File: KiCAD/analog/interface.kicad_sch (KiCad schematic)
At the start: 13 parts, among them J15 Screw_Terminal_01x03, J4 8P8C_Shielded, U16 AM26LS32ACN

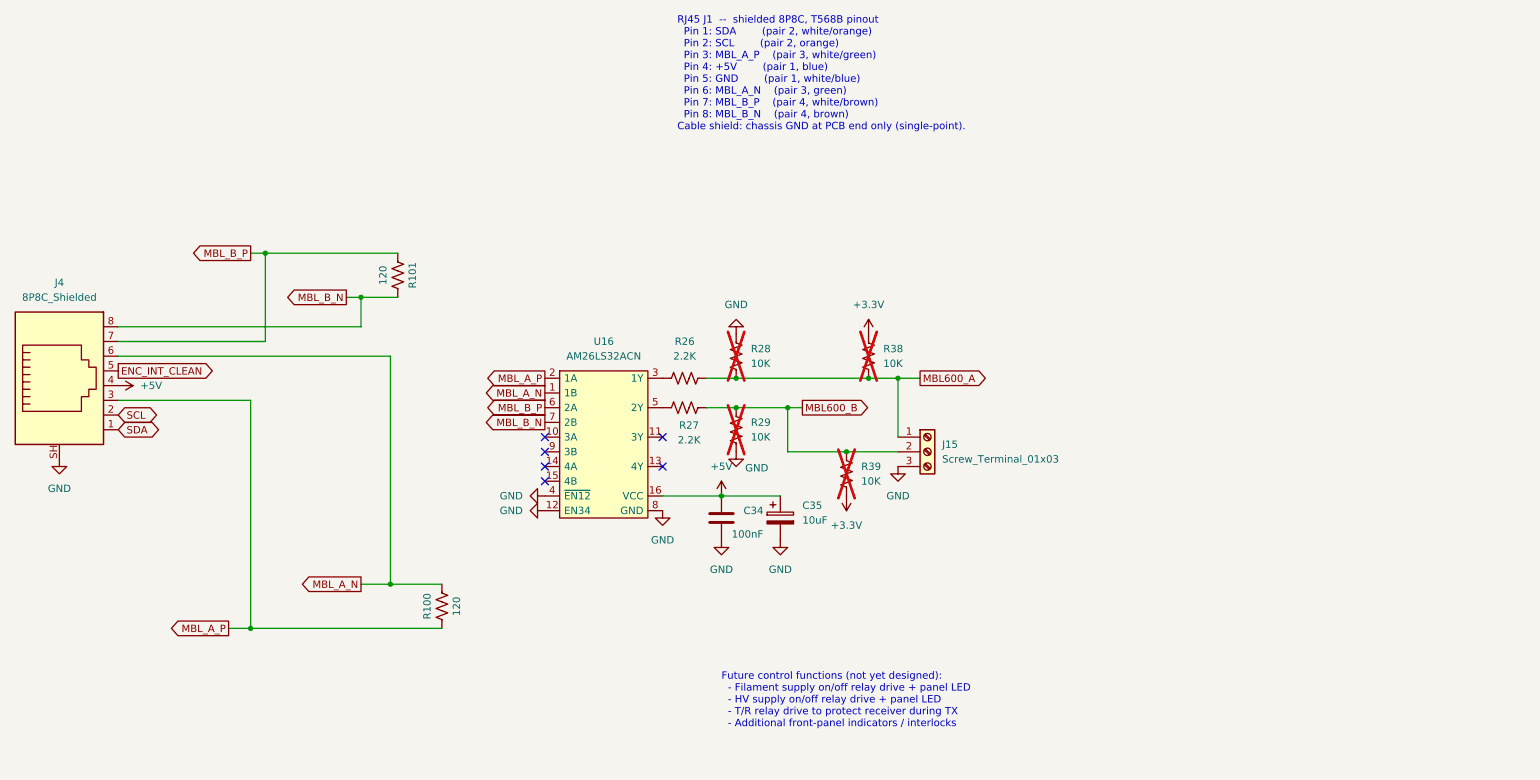
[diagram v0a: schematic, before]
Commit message: revD analog: L1 Bourns 78F footprint + CD74HC4050E xmitter lib additions
Analog L1 (270nH Bourns 78F RF choke) gets footprint
Inductor_THT:L_Axial_L7.0mm_D3.3mm_P10.16mm_Horizontal_Fastron_MICC
(stock KiCad; 78F body 7.11x2.79mm fits within the MICC silk envelope).

Added to xmitter library:
- symbol CD74HC4050E (hex non-inverting buffer, DIP-16, standard 4050
  pinout, pre-linked to xmitter:DIP-16_W7.62mm footprint)
- footprint xmitter:DIP-16_W7.62mm (verbatim copy of stock
  Package_DIP:DIP-16_W7.62mm so the lib is self-contained)

Other sheet / project / netlist touches picked up from the recent
session work on analog test sheet and protoshield.

Co-Authored-By: Claude Opus 4.7 <noreply@anthropic.com>
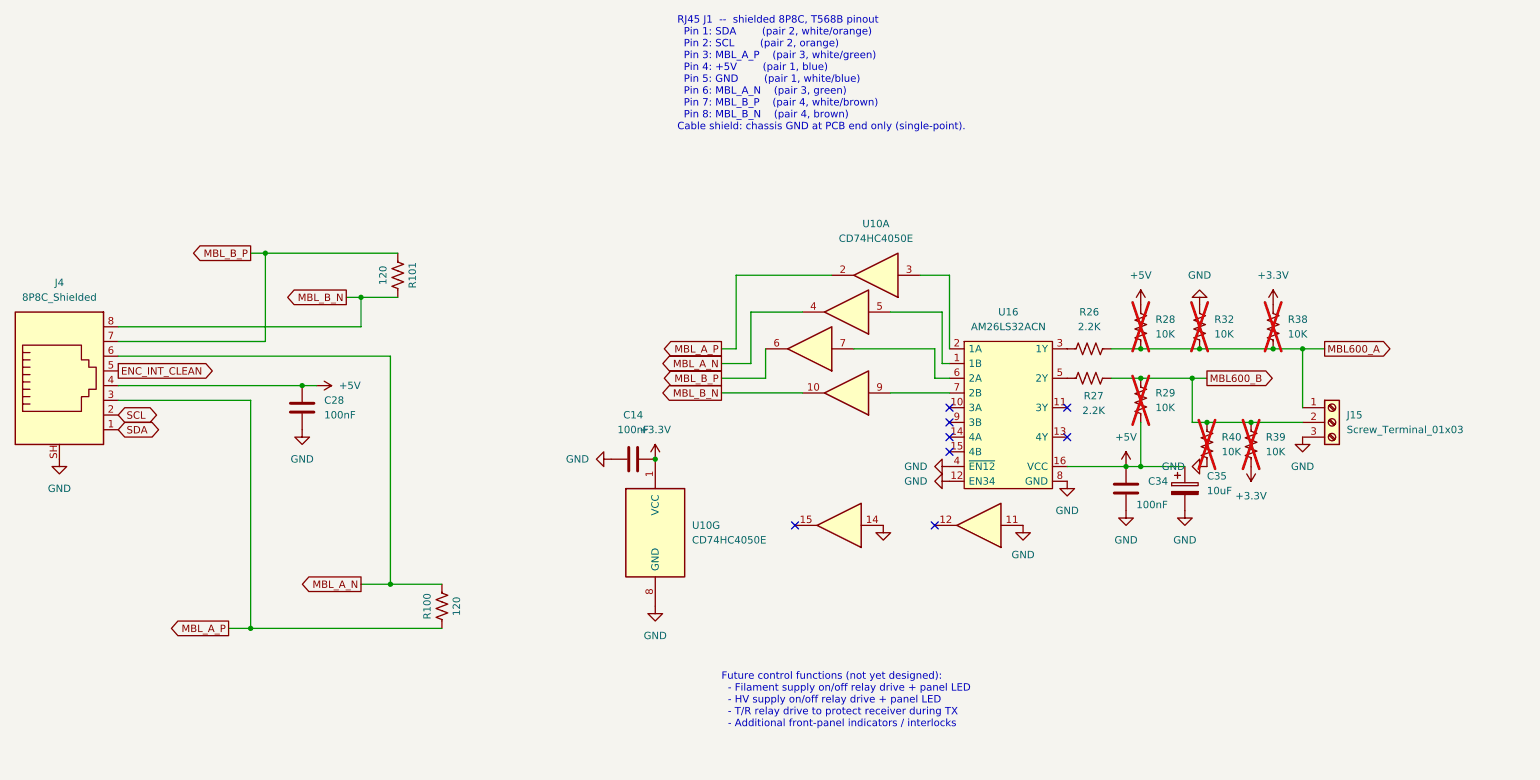
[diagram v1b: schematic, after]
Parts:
- added C14, C28: 100nF, symbol Device:C
- added R32, R40: 10K, Resistor_THT:R_Axial_DIN0207_L6.3mm_D2.5mm_P10.16mm_Horizontal, symbol Device:R_US
- added U10: CD74HC4050E, xmitter:DIP-16_W7.62mm, symbol xmitter:CD74HC4050E
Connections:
- net +3.3V: now also C14.2, U10.1 (VCC)
- net +5V: now also R28.1, R29.2, C28.1
- net GND: now also C14.1, C28.2, R32.1, R40.2, U10.11, U10.14, U10.8 (GND); no longer R28.1, R29.2
- net MBL600_A: now also R32.2
- net MBL600_B: now also R40.1
- net MBL_A_N: now also U10.4; no longer U16.1 (1B)
- net MBL_A_P: now also U10.2; no longer U16.2 (1A)
- net MBL_B_N: now also U10.10; no longer U16.7 (2B)
- net MBL_B_P: now also U10.6; no longer U16.6 (2A)
- new net: U10.3, U16.2 (1A)
- new net: U10.9, U16.7 (2B)
- new net: U10.5, U16.1 (1B)
- new net: U10.7, U16.6 (2A)
- no-connect marks 6 -> 8
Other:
- moved on the sheet: C34, C35, J15, R26, R27, R28, R29, R38, R39, U16

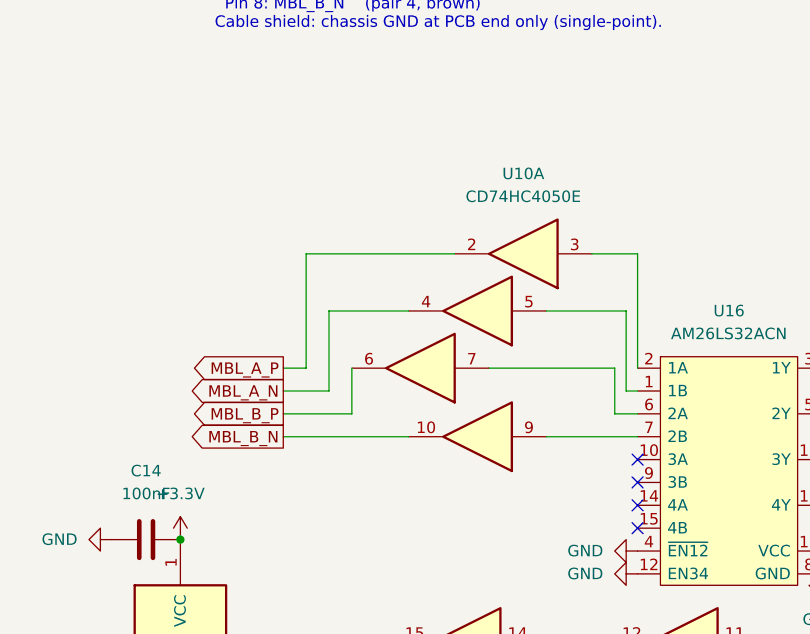
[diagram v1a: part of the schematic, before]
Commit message: revD: ss_pa U13 LM2936 pinout fix + analog U9 74HCT125 miswiring fix
ss_pa fault_shutdown.kicad_sch: fix U13 pin-to-signal mapping so an
LM2936Z-5.0/NOPB can be installed without destruction (prior MCP1700
symbol had pin 1=GND, 2=VI, 3=VO; LM2936 datasheet is pin 1=VO, 2=GND,
3=VI).

analog dac.kicad_sch: fix U9 74HCT125 miswiring found during follow-up
audit.

Co-Authored-By: Claude Opus 4.7 <noreply@anthropic.com>
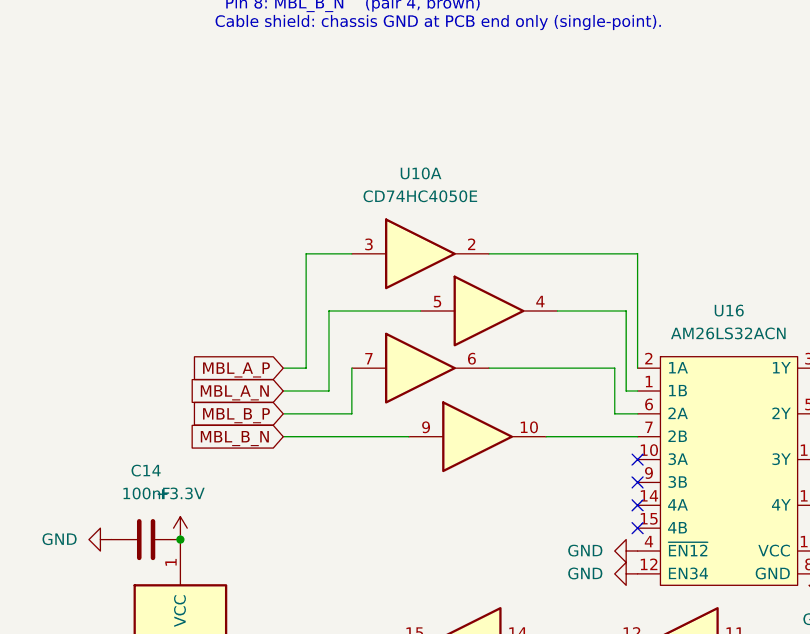
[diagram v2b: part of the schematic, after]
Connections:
- net MBL_A_N: now also U10.5; no longer U10.4
- net MBL_A_P: now also U10.3; no longer U10.2
- net MBL_B_N: now also U10.9; no longer U10.10
- net MBL_B_P: now also U10.7; no longer U10.6
- net at U16.2 (1A): now also U10.2; no longer U10.3
- net at U16.7 (2B): now also U10.10; no longer U10.9
- net at U16.1 (1B): now also U10.4; no longer U10.5
- net at U16.6 (2A): now also U10.6; no longer U10.7

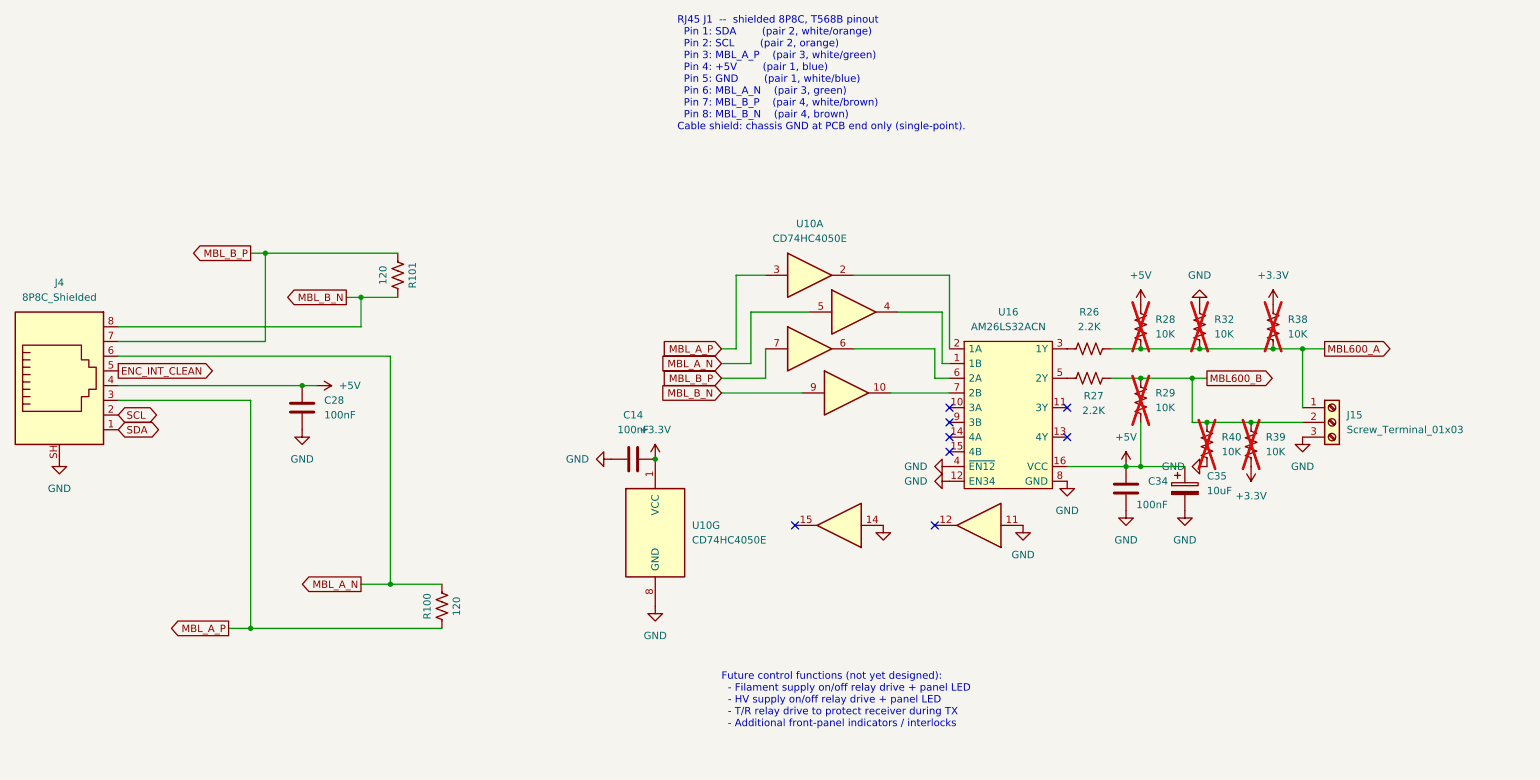
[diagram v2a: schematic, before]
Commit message: revD: footprint pass across all boards + ss_pa fault-chain fix + LLM review brief
- New tools/assign_misc_footprints.py: lib_id-keyed footprint assigner
  (resistors, screw terminals, pin headers, LT1054); mirrors cap-script
  safe-write (UTF-8 no BOM, no CRLF translation).
- tools/assign_cap_footprints.py: added 0.47uF -> C_Rect_L7.0mm case.
- Ran both scripts across analog, ss_pa, Output LPF, frontpanel,
  protoshield, and shelved power board. ~100 fills; details in diffs.
- ss_pa: R1-R4 (0.22 ohm source sense) upgraded to 2W Yageo RSF200
  with DIN0516 L15.5mm/P20.32mm footprint; Value tagged "0.22R 2W".
  R15/R16 confirmed 1/4W (DIN0207) for BS170 source degeneration.
- analog/power: R44 15R 5W horizontal, P30.48mm footprint.
- ss_pa fault chain (from external LLM review): R21/R22 raised
  10K -> 100K to restore self-latching loop gain; new R26 = 100K
  across C12 so cap discharges between power cycles (reliable reset).
  R26 footprint pending.
- Documentation/revD_llm_review_brief.md: new, comprehensive system
  description for external LLM deep-dive (function, component values,
  power dissipation, design flaws). References all five board netlists.

Co-Authored-By: Claude Opus 4.7 <noreply@anthropic.com>
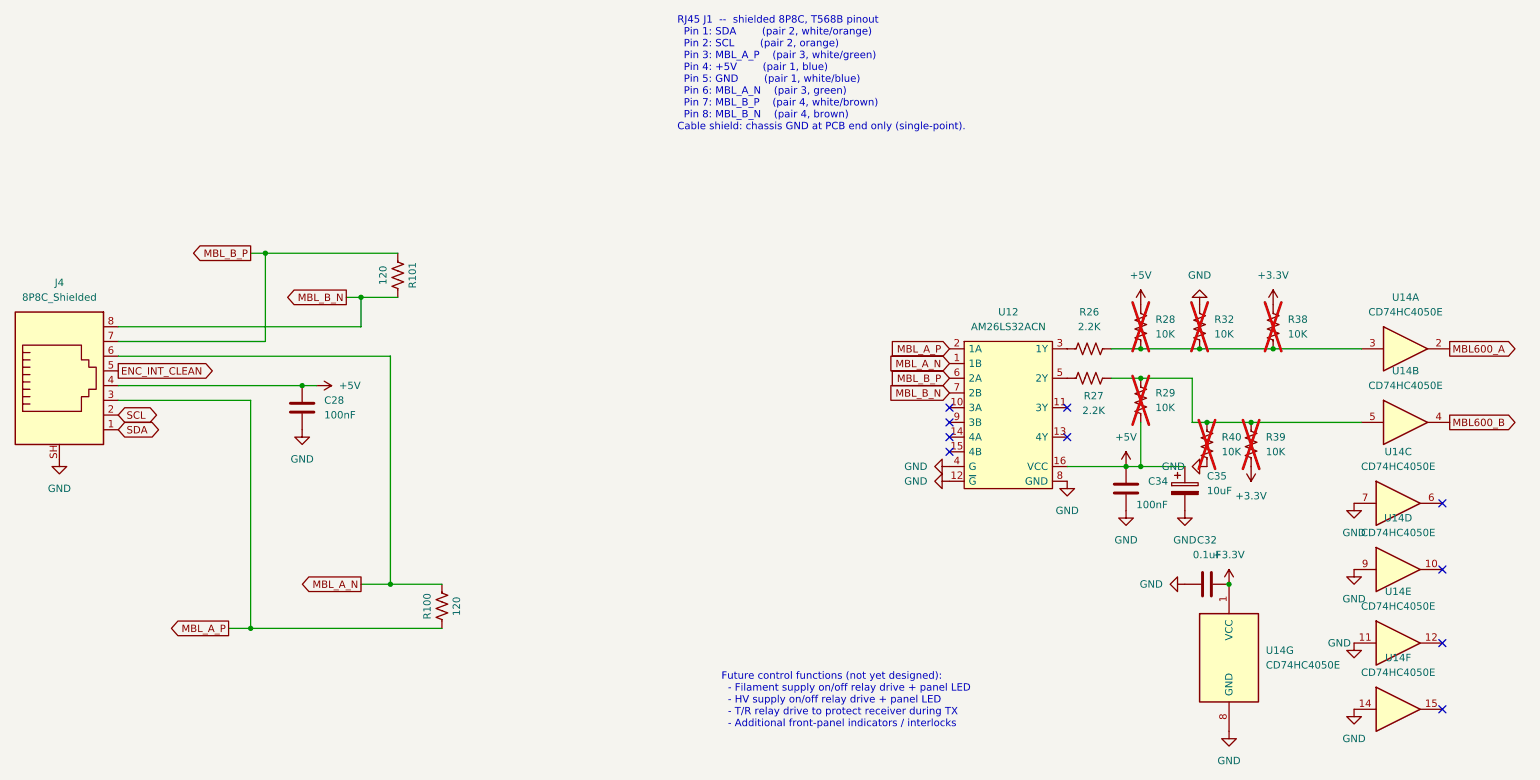
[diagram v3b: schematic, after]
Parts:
- removed C14: 100nF, symbol Device:C
- removed J15: Screw_Terminal_01x03, TerminalBlock_Phoenix:TerminalBlock_Phoenix_MKDS-1,5-3_1x03_P5.00mm_Horizontal, symbol Connector:Screw_Terminal_01x03
- removed U10: CD74HC4050E, xmitter:DIP-16_W7.62mm, symbol xmitter:CD74HC4050E
- removed U16: AM26LS32ACN, Package_DIP:DIP-16_W7.62mm, symbol xmitter:AM26LS32ACN
- added C32: 0.1uF, Capacitor_THT:C_Disc_D5.0mm_W2.5mm_P5.00mm, symbol Device:C
- added U12: AM26LS32ACN, Package_DIP:DIP-16_W7.62mm, symbol xmitter:AM26LS32ACN
- added U14: CD74HC4050E, xmitter:DIP-16_W7.62mm, symbol xmitter:CD74HC4050E
- C28: footprint (none) -> Capacitor_THT:C_Disc_D5.0mm_W2.5mm_P5.00mm
- R38, R39: footprint (none) -> Resistor_THT:R_Axial_DIN0207_L6.3mm_D2.5mm_P10.16mm_Horizontal
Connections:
- net +3.3V: now also C32.2, U14.1 (VCC)
- net +5V: now also U12.16 (VCC)
- net GND: now also C32.1, U12.12 (~{G}), U12.4 (G), U12.8 (GND), U14.11, U14.14, U14.7, U14.8 (GND), U14.9
- net MBL600_A: now also U14.2; no longer R26.2, R28.2, R32.2, R38.2
- net MBL600_B: now also U14.4; no longer R27.2, R29.1, R39.1, R40.1
- net MBL_A_N: now also U12.1 (1B)
- net MBL_A_P: now also U12.2 (1A)
- net MBL_B_N: now also U12.7 (2B)
- net MBL_B_P: now also U12.6 (2A)
- net at R26.1: now also U12.3 (1Y)
- net at R27.1: now also U12.5 (2Y)
- new net: R26.2, R28.2, R32.2, R38.2, U14.3
- new net: R27.2, R29.1, R39.1, R40.1, U14.5
- no-connect marks 8 -> 10

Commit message: revD: front panel absorbed into analog as sub-sheet
- front_panel.kicad_sch (new): front-panel circuitry pulled onto
  the analog board as a hierarchical sub-sheet; eliminates the
  separate frontpanel PCB (board count now 3: analog, ss_pa,
  Output LPF)
- analog.kicad_sch: new sub-sheet reference for Front_Panel
- interface.kicad_sch: rewired to connect to the local
  Front_Panel sheet instead of the former RJ45 umbilical
- analog.net regenerated

NOTE: KiCAD/frontpanel/ directory still present on disk; will be
removed in a later cleanup commit once the absorbed version is
verified ERC-clean.

Co-Authored-By: Claude Opus 4.7 <noreply@anthropic.com>
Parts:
- removed C28: 100nF, Capacitor_THT:C_Disc_D5.0mm_W2.5mm_P5.00mm, symbol Device:C
- removed J4: 8P8C_Shielded, xmitter:Amphenol_RJE1D-188_Horizontal_Shielded, symbol Connector:8P8C_Shielded
- removed R100, R101: 120, Resistor_THT:R_Axial_DIN0207_L6.3mm_D2.5mm_P10.16mm_Horizontal, symbol Device:R_US
- added C58: 100nF, Capacitor_THT:C_Disc_D5.0mm_W2.5mm_P5.00mm, symbol Device:C
- added C59: 10uF, Capacitor_THT:CP_Radial_D5.0mm_P2.00mm, symbol Device:C_Polarized
- added ENC5: Encoder_5734, Connector_PinHeader_2.54mm:PinHeader_1x06_P2.54mm_Vertical, symbol xmitter:Encoder_5734
- added R57, R58: 120R, symbol Device:R_US
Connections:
- net +5V: now also C58.2, C59.1, ENC5.4 (VCC)
- net GND: now also C58.1, C59.2, ENC5.3 (GND)
- net MBL_A_N: now also ENC5.5 (A-), R57.2
- net MBL_A_P: now also ENC5.1 (A+), R57.1
- net MBL_B_N: now also ENC5.6 (B-), R58.2
- net MBL_B_P: now also ENC5.2 (B+), R58.1
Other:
- note added: "No test point for this encoder since access is easy through connector"
